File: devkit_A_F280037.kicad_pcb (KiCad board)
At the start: 2 copper layers, 64 x 28 mm, 0 parts

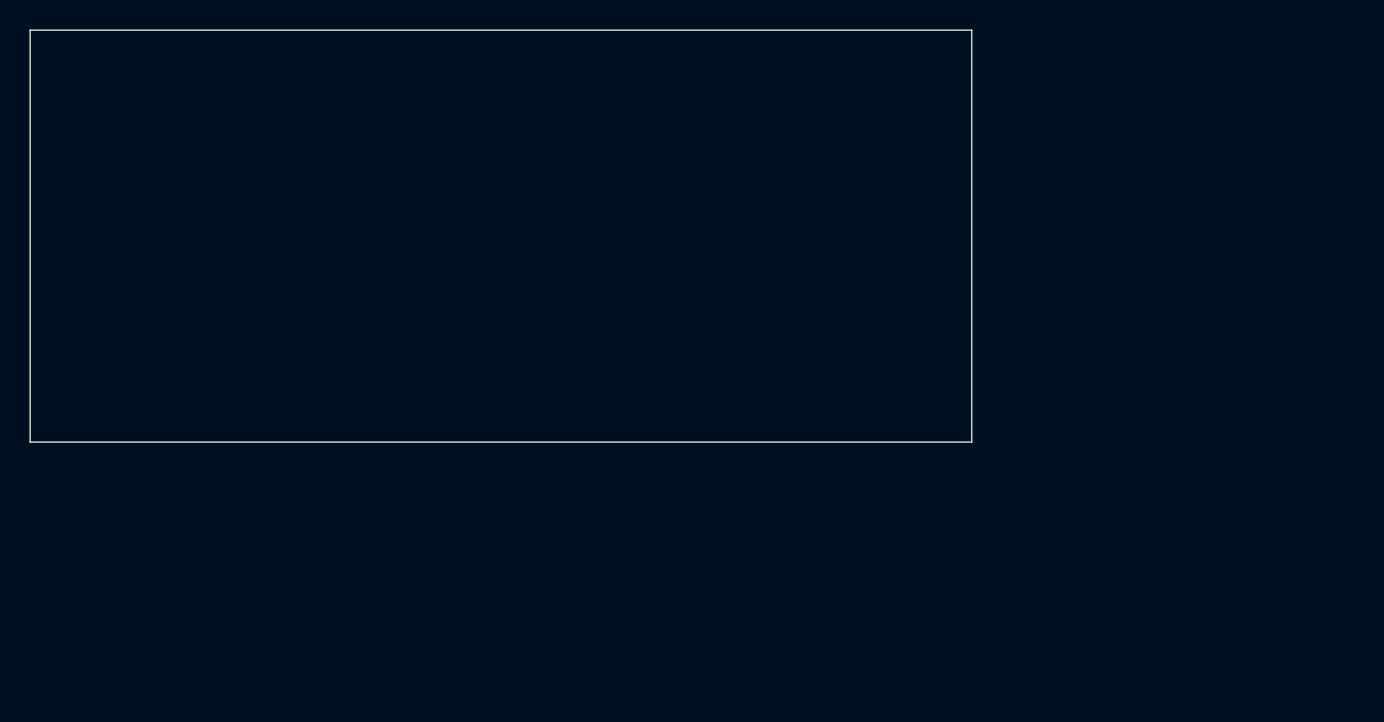
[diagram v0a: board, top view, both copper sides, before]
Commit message: Renomme par groupe: kicad_gen commun, gen_*.py, projets shield/shield_2x24/devkit_A/devkit_B, doc/
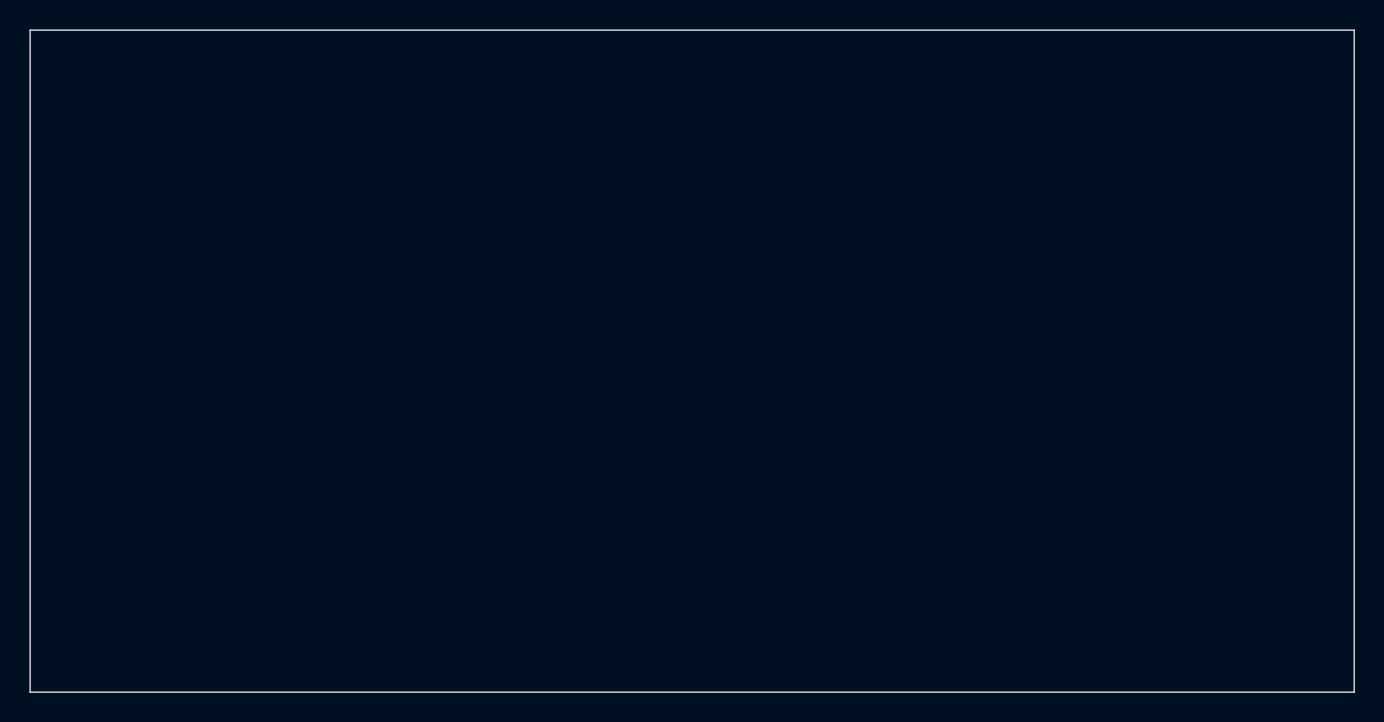
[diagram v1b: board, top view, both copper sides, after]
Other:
- board size 64 x 28 mm -> 90 x 45 mm
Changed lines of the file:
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@@
 (kicad_pcb
 	(version 20241229)
-	(generator "projet_gen")
+	(generator "kicad_gen")
 	(generator_version "1.0")
 	(general
@@
 	)
 	(net 0 "")
-	(gr_line (start 100.000 80.000) (end 164.000 80.000)
+	(gr_line (start 100.000 80.000) (end 190.000 80.000)
 		(stroke (width 0.1) (type default)) (layer "Edge.Cuts")
 	)
-	(gr_line (start 164.000 80.000) (end 164.000 108.000)
+	(gr_line (start 190.000 80.000) (end 190.000 125.000)
 		(stroke (width 0.1) (type default)) (layer "Edge.Cuts")
 	)
-	(gr_line (start 164.000 108.000) (end 100.000 108.000)
+	(gr_line (start 190.000 125.000) (end 100.000 125.000)
 		(stroke (width 0.1) (type default)) (layer "Edge.Cuts")
 	)
-	(gr_line (start 100.000 108.000) (end 100.000 80.000)
+	(gr_line (start 100.000 125.000) (end 100.000 80.000)
 		(stroke (width 0.1) (type default)) (layer "Edge.Cuts")
 	)
